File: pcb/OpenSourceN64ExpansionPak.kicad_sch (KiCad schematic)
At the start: 24 parts, among them U1 MSM5718B70-60GS-K, U2 MSM5718B70-60GS-K

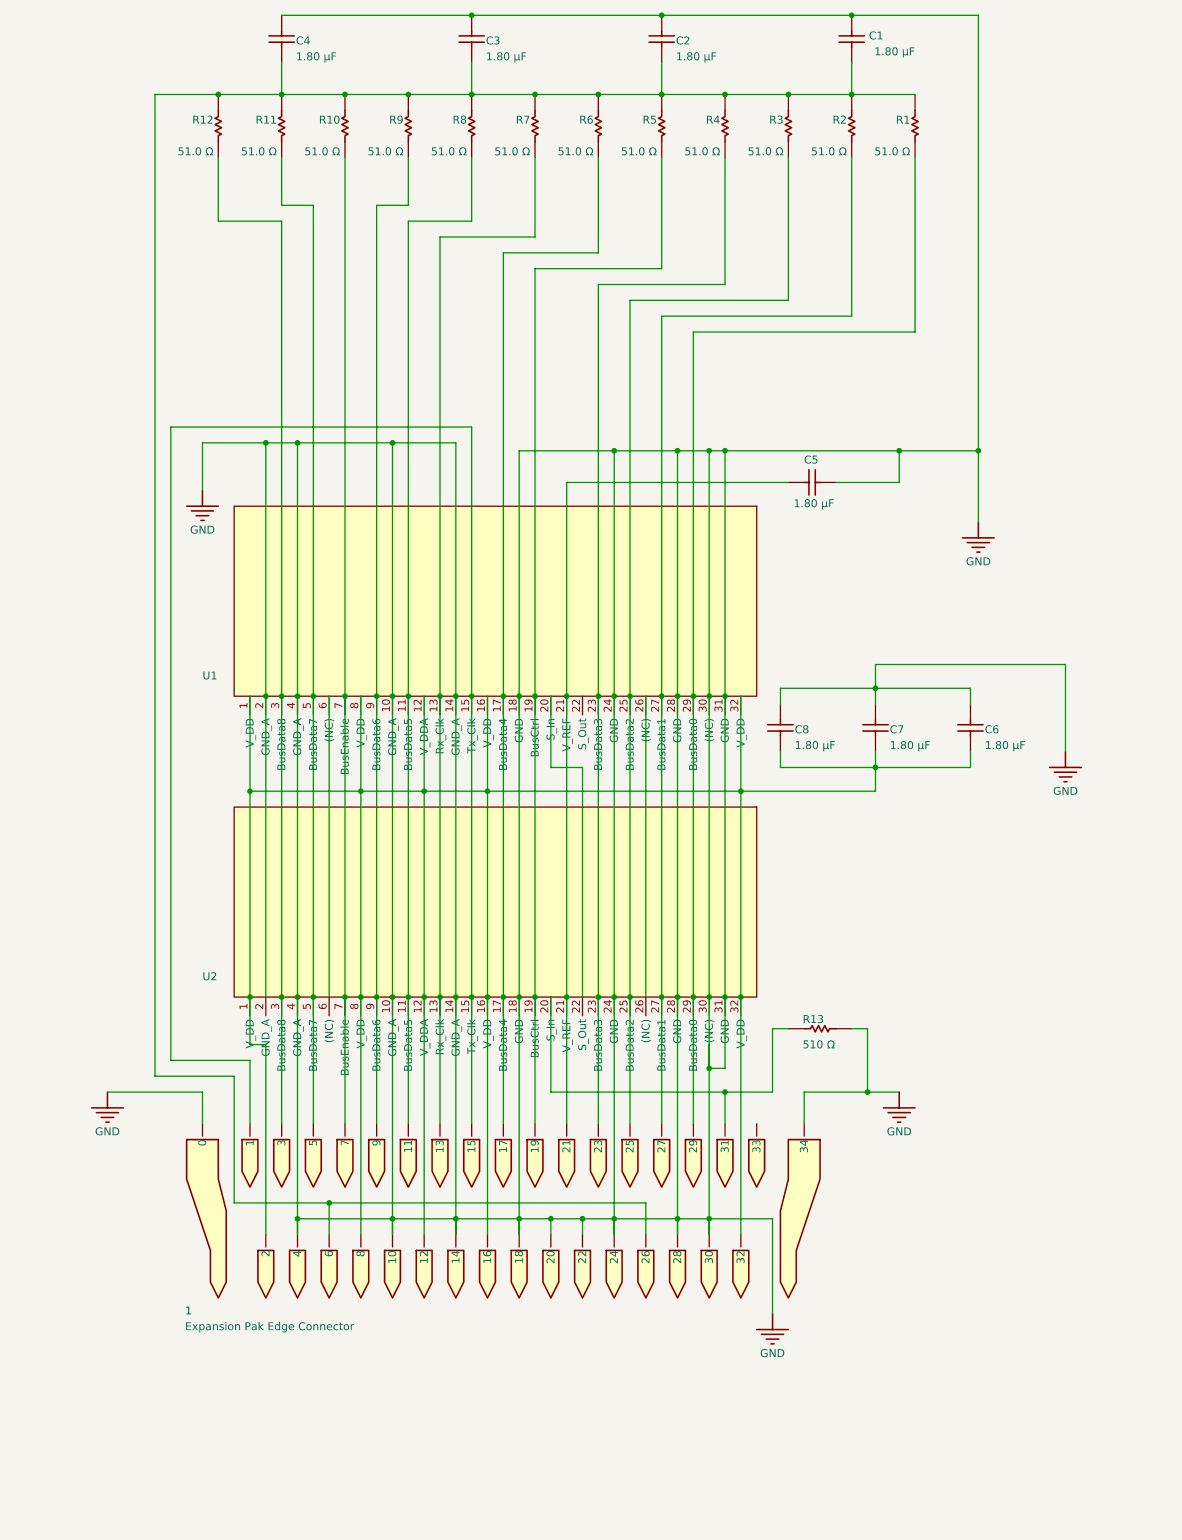
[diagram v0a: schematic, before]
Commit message: Fix N64 Killer and more
- License change from CERN-OHL-P-2.0 and MIT to Attribution-NonCommercial-ShareAlike (CC BY-NC-SA 4.0) (No commercial use of this version is allowed.)
- Reworked the cart edge connector to be asymetrical, same as the original one
- Cleanup PCB layout
- Swap from single resistors to resistor arrays
- Add jumpers to allow for different configurations
- Reworked the 3D shell design
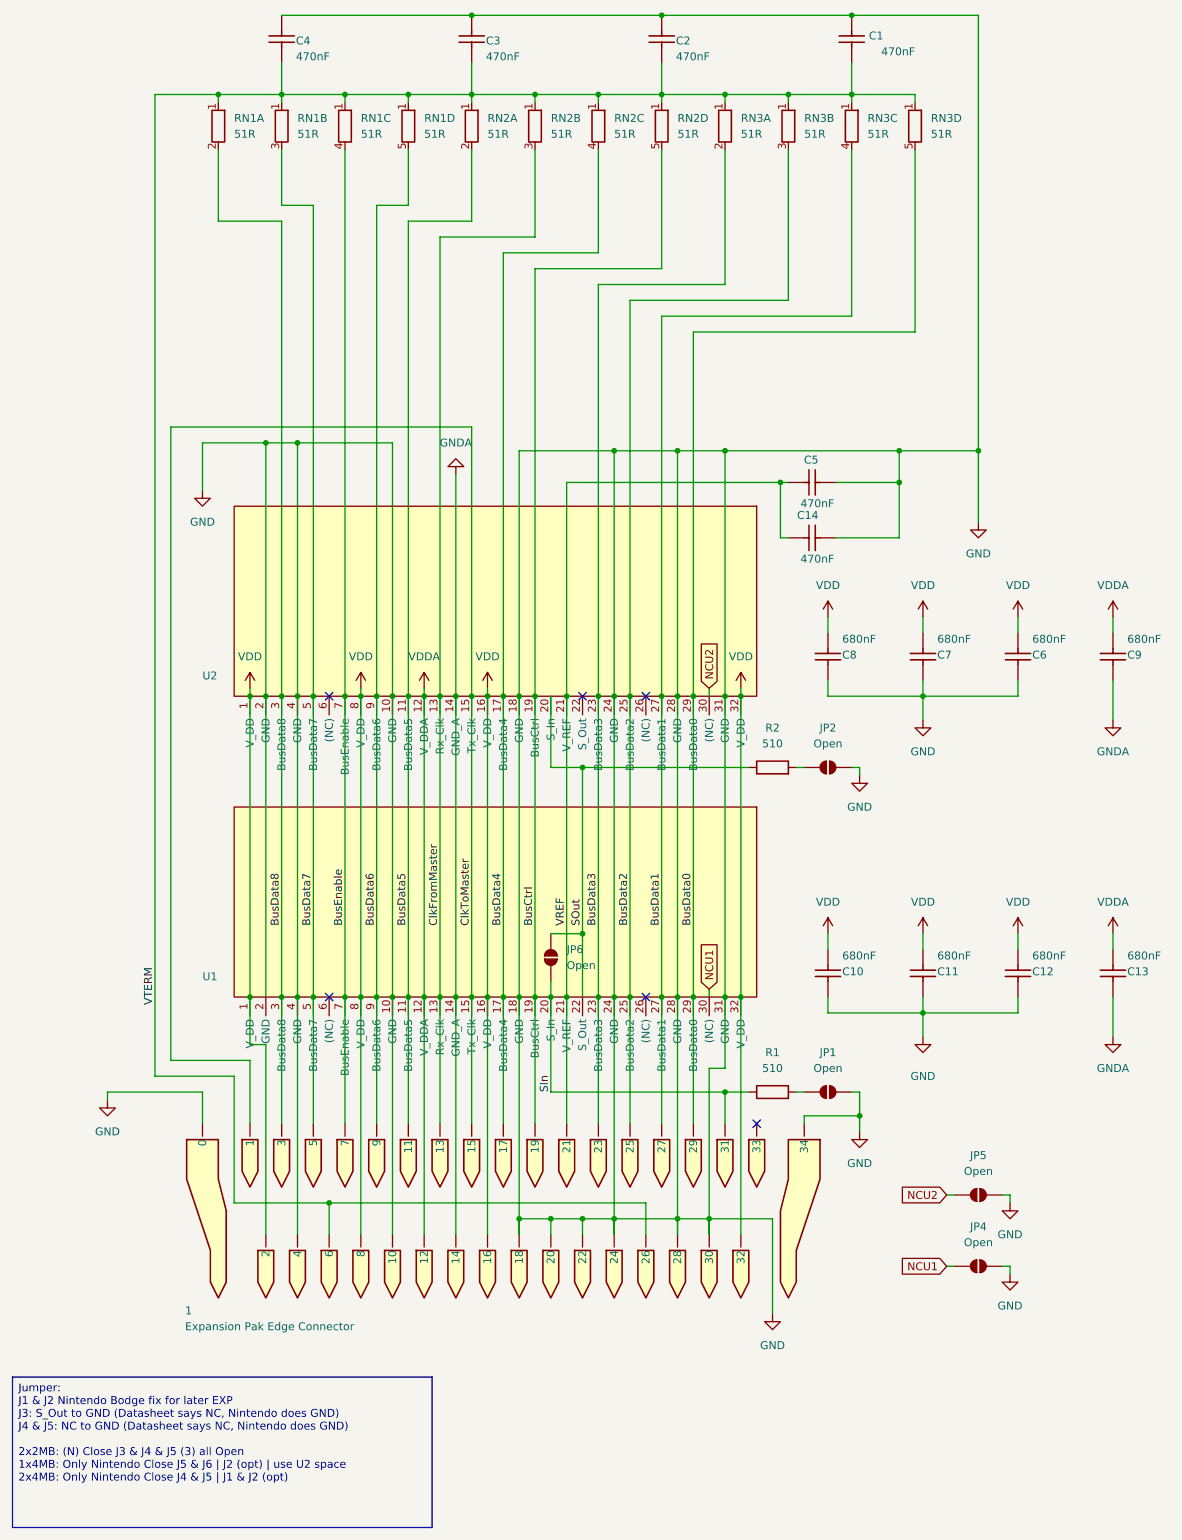
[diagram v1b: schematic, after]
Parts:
- removed R1, R10, R11, R12, R2, R3, R4, R5, R6, R7, R8, R9: 51Y, Resistor_SMD:R_0805_2012Metric_Pad1.20x1.40mm_HandSolder, symbol OpenSourceN64ExpansionPak-altium-import:1_RES-2
- removed R13: Yageo RC0805FR-07510RL, Resistor_SMD:R_0805_2012Metric_Pad1.20x1.40mm_HandSolder, symbol OpenSourceN64ExpansionPak-altium-import:0_RES-2
- removed U2: MSM5718B70-60GS-K, ExpansionPak:RAM Module, symbol OpenSourceN64ExpansionPak-altium-import:1_MSM5718B70-60GS-K-Symbol-1
- added C10, C11, C12, C13, C9: 680nF, Capacitor_SMD:C_0603_1608Metric, symbol Symbols:1_SYM-94265da154d84be1-1
- added C14: 470nF, Capacitor_SMD:C_0603_1608Metric, symbol Symbols:1_SYM-94265da154d84be1-1
- added JP1, JP2, JP4, JP5, JP6: Open, Footprints:SolderJumper-tiny, symbol Symbols:SolderJumper_2_Open
- added R1, R2: 510, Resistor_SMD:R_0603_1608Metric, symbol Symbols:R
- added RN1, RN2, RN3: 51R, Footprints:R_Array_Convex_4x0603_common, symbol Symbols:R_Network04_Split
- added U2: MSM5718B70-60GS-K, Footprints:N64_RDRAM, symbol Symbols:1_MSM5718B70-60GS-K-Symbol-1_1
- 1: footprint ExpansionPak:EdgeConnector -> Footprints:N64_Expansion_Edge_Connector; symbol OpenSourceN64ExpansionPak-altium-import:0_Expansion Pak Edge Connector-Symbol-1 -> Symbols:0_Expansion Pak Edge Connector-Symbol-1
- C1, C2, C3, C4, C5: value ~ -> 470nF; footprint Capacitor_SMD:C_0805_2012Metric_Pad1.18x1.45mm_HandSolder -> Capacitor_SMD:C_0603_1608Metric; symbol OpenSourceN64ExpansionPak-altium-import:1_SYM-94265da154d84be1-1 -> Symbols:1_SYM-94265da154d84be1-1; CAPACITANCE 1.80 µF -> 470nF; LCSC (none) -> C1623
- C6, C7, C8: value ~ -> 680nF; footprint Capacitor_SMD:C_0805_2012Metric_Pad1.18x1.45mm_HandSolder -> Capacitor_SMD:C_0603_1608Metric; symbol OpenSourceN64ExpansionPak-altium-import:1_SYM-94265da154d84be1-1 -> Symbols:1_SYM-94265da154d84be1-1; CAPACITANCE 1.80 µF -> 680nF; LCSC (none) -> C327005
- U1: footprint ExpansionPak:RAM Module -> Footprints:N64_RDRAM; symbol OpenSourceN64ExpansionPak-altium-import:1_MSM5718B70-60GS-K-Symbol-1 -> Symbols:1_MSM5718B70-60GS-K-Symbol-1_1
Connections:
- net GND: now also C10.2, C11.2, C12.2, C14.1, JP1.2 (B), JP2.2 (B), JP4.2 (B), JP5.2 (B), U2.10 (GND), U2.18 (GND), U2.2 (GND), U2.24 (GND), U2.28 (GND), U2.31 (GND), U2.4 (GND); no longer 1.14, U1.14 (GND_A), U1.30 ((NC))
- net VTERM: now reaches 1.26, 1.6, C1.2, C2.1, C3.1, C4.1
- net VTERM: now also RN1.1 (R1), RN1.1 (R1), RN1.1 (R1), RN1.1 (R1), RN2.1 (R1), RN2.1 (R1), RN2.1 (R1), RN2.1 (R1), RN3.1 (R1), RN3.1 (R1), RN3.1 (R1), RN3.1 (R1)
- net BusData2: now reaches 1.25, U1.25 (BusData2)
- net BusData2: now also RN3.3 (R2.2), U2.25 (BusData2)
- net ClkFromMaster: now reaches 1.13, U1.13 (Rx_Clk)
- net ClkFromMaster: now also RN2.3 (R2.2), U2.13 (Rx_Clk)
- net VDD: now reaches 1.16, 1.2, 1.32, 1.8, C6.1, C7.1, C8.1, U1.1 (V_DD), U1.16 (V_DD), U1.32 (V_DD), U1.8 (V_DD)
- net VDD: now also C10.1, C11.1, C12.1, U2.1 (V_DD), U2.16 (V_DD), U2.32 (V_DD), U2.8 (V_DD); no longer 1.12, U1.12 (V_DDA)
- net BusData5: now reaches 1.11, U1.11 (BusData5)
- net BusData5: now also RN2.2 (R1.2), U2.11 (BusData5)
- net ClkToMaster: now reaches 1.1, 1.15, U1.15 (Tx_Clk)
- net ClkToMaster: now also U2.15 (Tx_Clk)
- net BusData4: now reaches 1.17, U1.17 (BusData4)
- net BusData4: now also RN2.4 (R3.2), U2.17 (BusData4)
- net BusCtrl: now reaches 1.19, U1.19 (BusCtrl)
- net BusCtrl: now also RN2.5 (R4.2), U2.19 (BusCtrl)
- net SIn: now reaches U1.20 (S_In)
- net SIn: now also 1.31, JP6.1 (A), R1.1
- net VREF: now reaches 1.21, C5.2, U1.21 (V_REF)
- net VREF: now also C14.2, U2.21 (V_REF)
- net SOut: now reaches U1.22 (S_Out)
- net SOut: now also JP6.2 (B), R2.1, U2.20 (S_In)
- net BusData3: now reaches 1.23, U1.23 (BusData3)
- net BusData3: now also RN3.2 (R1.2), U2.23 (BusData3)
- net BusData1: now reaches 1.27, U1.27 (BusData1)
- net BusData1: now also RN3.4 (R3.2), U2.27 (BusData1)
- net BusData0: now reaches 1.29, U1.29 (BusData0)
- net BusData0: now also RN3.5 (R4.2), U2.29 (BusData0)
- net BusData8: now reaches 1.3, U1.3 (BusData8)
- net BusData8: now also RN1.2 (R1.2), U2.3 (BusData8)
- net BusData7: now reaches 1.5, U1.5 (BusData7)
- net BusData7: now also RN1.3 (R2.2), U2.5 (BusData7)
- net BusEnable: now reaches 1.7, U1.7 (BusEnable)
- net BusEnable: now also RN1.4 (R3.2), U2.7 (BusEnable)
- net BusData6: now reaches 1.9, U1.9 (BusData6)
- net BusData6: now also RN1.5 (R4.2), U2.9 (BusData6)
- new net: JP1.1 (A), R1.2
- new net: JP2.1 (A), R2.2
- new net GNDA: 1.14, C13.2, C9.2, U1.14 (GND_A), U2.14 (GND_A)
- new net NCU1: JP4.1 (A), U1.30 ((NC))
- new net NCU2: JP5.1 (A), U2.30 ((NC))
- new net VDDA: 1.12, C13.1, C9.1, U1.12 (V_DDA), U2.12 (V_DDA)
- no-connect marks 0 -> 6
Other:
- moved on the sheet: C6, C7, C8, U1
